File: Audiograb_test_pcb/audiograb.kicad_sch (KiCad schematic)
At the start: 7 parts, among them J1 USB_C_Receptacle_USB2.0_16P, J20 JST-TH, U12 IP4220CZ6F

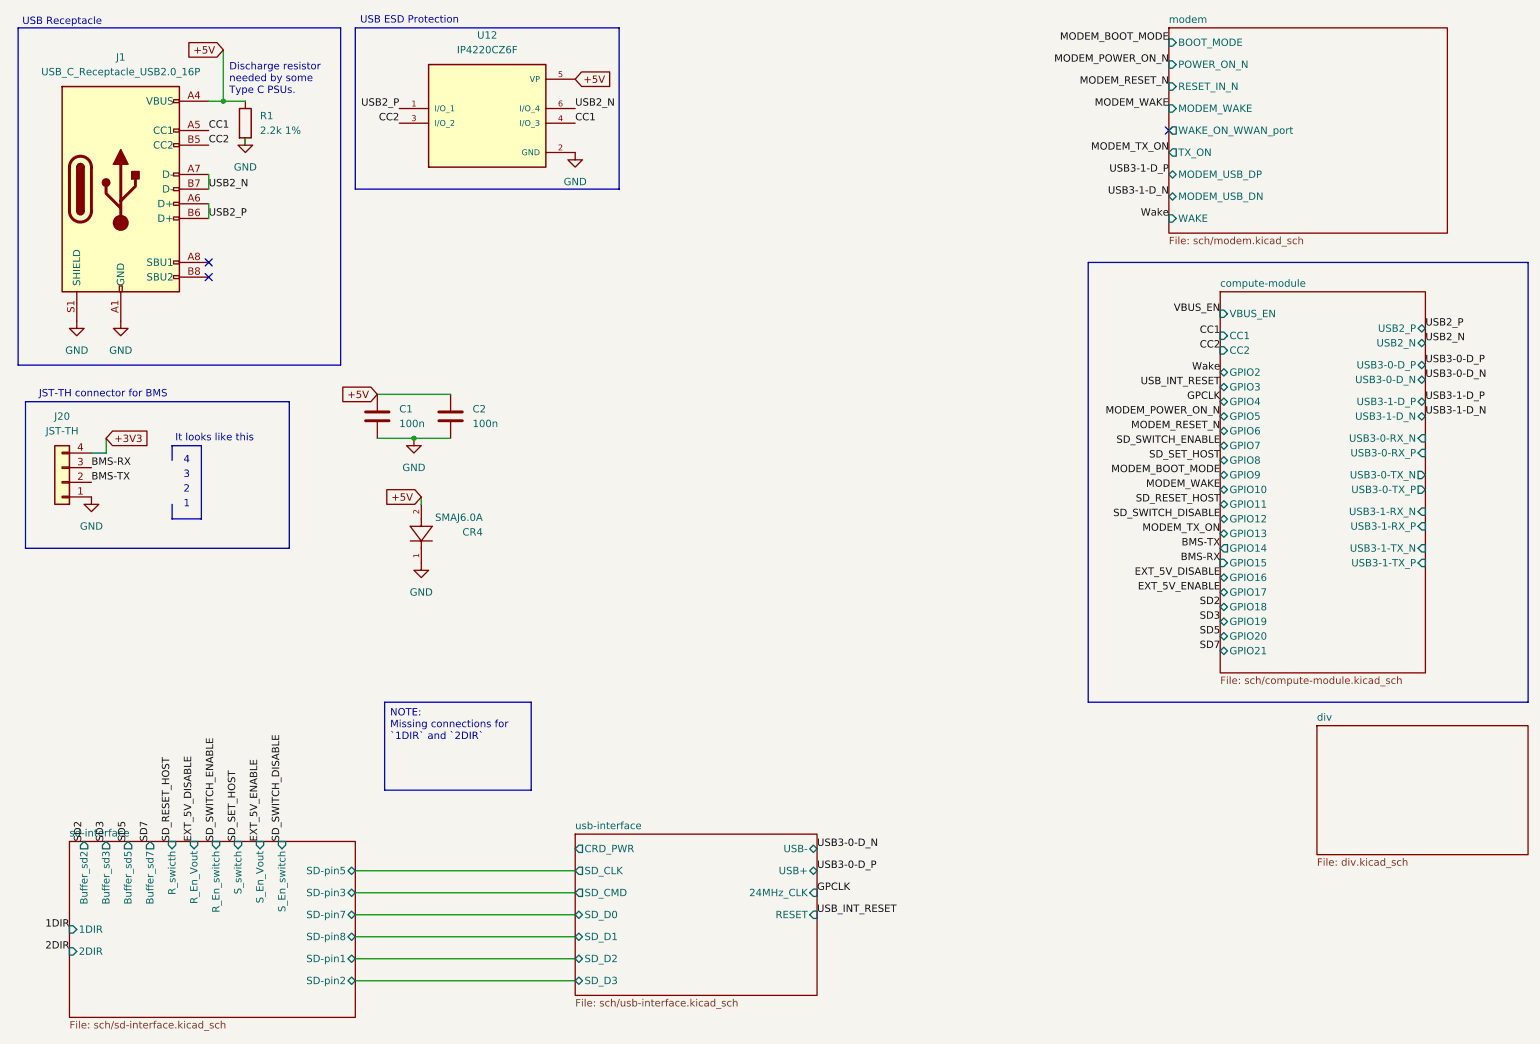
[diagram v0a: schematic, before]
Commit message: La til hard shutdown for modem, la til signal SAFE_PWR_REMOVE, fikset nummerering testpoints ++ noen småting
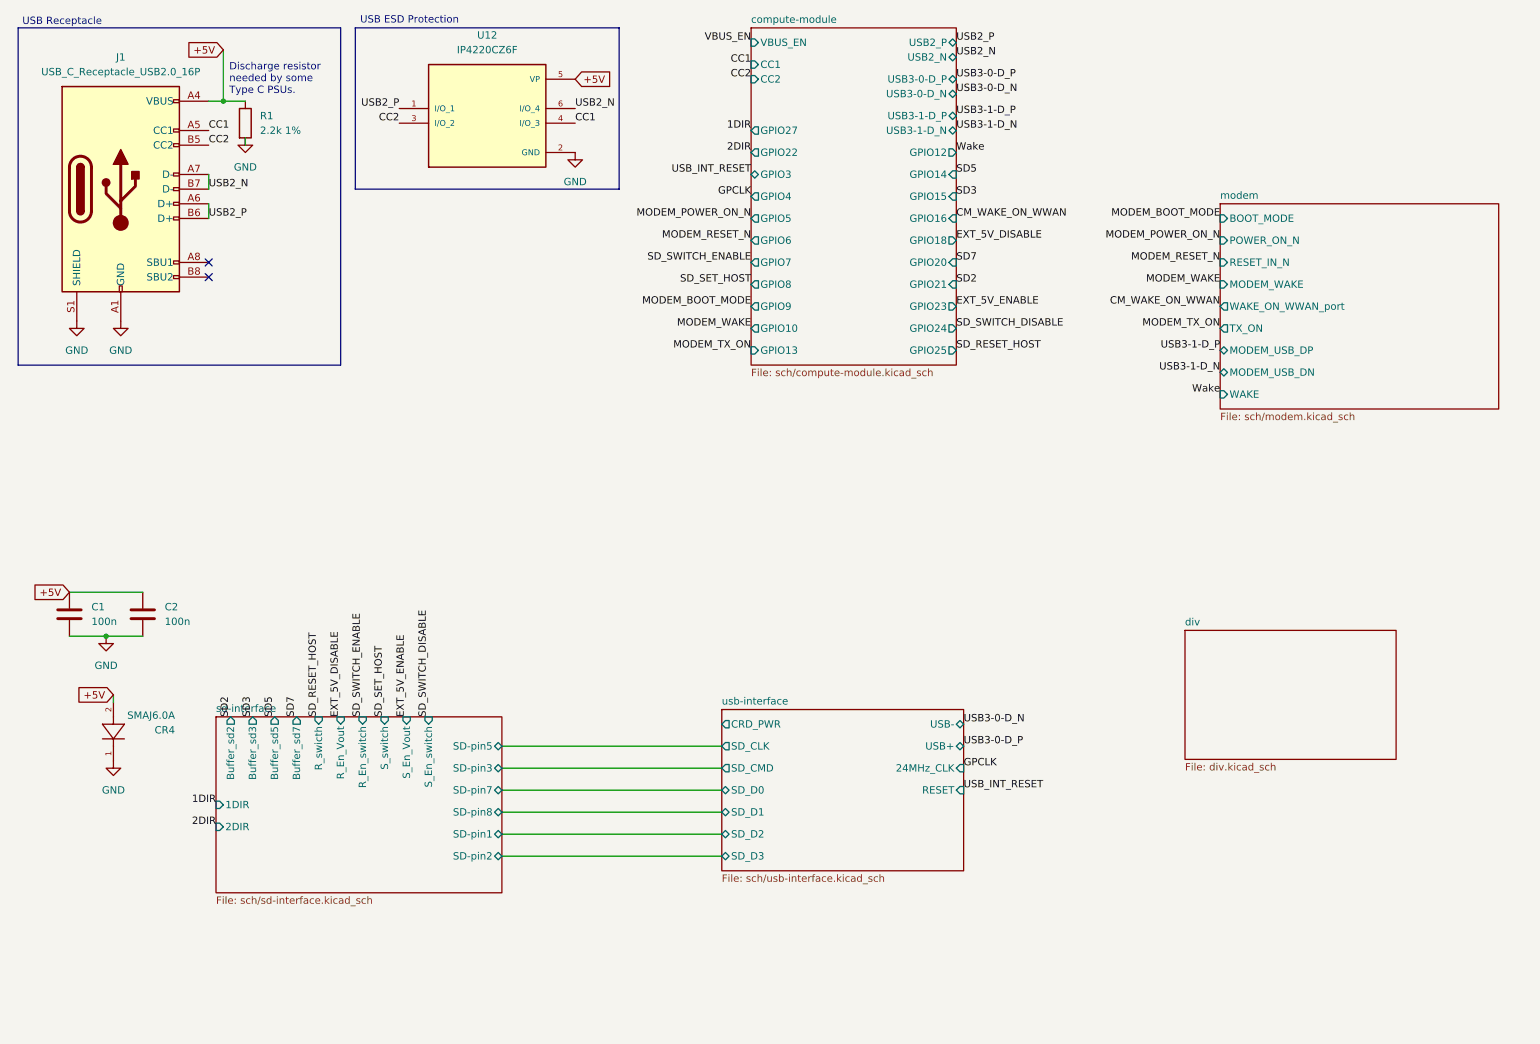
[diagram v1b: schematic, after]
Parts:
- removed J20: JST-TH, 4ms_Connector:Pins_1x04_2.54mm_TH_SWD, symbol PCM_4ms_Connector:Conn_01x04
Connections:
- no-connect marks 3 -> 2
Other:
- sheet compute-module ports: added GPIO22, GPIO23, GPIO24, GPIO25, GPIO27; removed GPIO11, GPIO17, GPIO19, GPIO2, USB3-0-RX_N, USB3-0-RX_P, USB3-0-TX_N, USB3-0-TX_P, USB3-1-RX_N, USB3-1-RX_P, USB3-1-TX_N, USB3-1-TX_P
- note removed: "1"
- note removed: "2"
- note removed: "3"
- note removed: "4"
- note removed: "It looks like this"
- note removed: "JST-TH connector for BMS"
- moved on the sheet: C1, C2, CR4
